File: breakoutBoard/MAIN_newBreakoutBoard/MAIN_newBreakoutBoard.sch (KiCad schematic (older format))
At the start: 3 parts, among them J1 Conn_02x06_Test_Pins, J2 Conn_02x06_Steering_Wheel_Qui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, J3 Conn_01x14

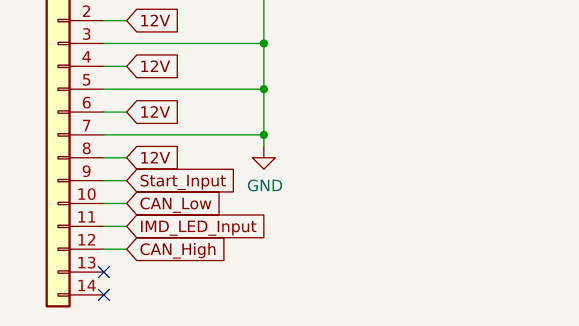
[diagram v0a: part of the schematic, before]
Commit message: Made use of entire ampseal connector
Had a late night ah ha momment;; Figured I would make use of all the pins on the ampseal connect and make it so we have the option to add another CAN node at the front of the car if need be.
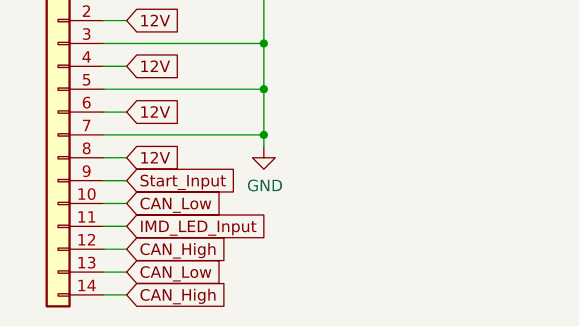
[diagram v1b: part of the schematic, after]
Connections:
- net CAN_High: now also J3.14 (Pin_14)
- net CAN_Low: now also J3.13 (Pin_13)
- no-connect marks 2 -> 0
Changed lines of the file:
@@
 EESchema Schematic File Version 4
+LIBS:MAIN_newBreakoutBoard-cache
 EELAYER 30 0
 EELAYER END
@@
 	0    -1   -1   0
 $EndComp
+Text GLabel 1400 3800 1    50   Input ~ 0
+12V
+Text GLabel 1800 3800 1    50   Input ~ 0
+CAN_Low
+Text GLabel 1900 3800 1    50   Input ~ 0
+CAN_High
+Text GLabel 1800 4500 3    50   Input ~ 0
+Start_Input
+Text GLabel 1900 4500 3    50   Input ~ 0
+IMD_LED_Input
+Wire Wire Line
+	1900 4500 1900 4400
+Wire Wire Line
+	1800 4500 1800 4400
+Wire Wire Line
+	1900 3800 1900 3900
+Wire Wire Line
+	1800 3800 1800 3900
+Wire Wire Line
+	1400 3800 1400 3850
+Wire Wire Line
+	1500 3900 1500 3850
+Wire Wire Line
+	1500 3850 1400 3850
+Connection ~ 1400 3850
+Wire Wire Line
+	1400 3850 1400 3900
+Wire Wire Line
+	1600 3900 1600 3850
+Wire Wire Line
+	1600 3850 1500 3850
+Connection ~ 1500 3850
+Wire Wire Line
+	1700 3900 1700 3850
+Wire Wire Line
+	1700 3850 1600 3850
+Connection ~ 1600 3850
+Wire Wire Line
+	1400 4500 1400 4450
+Wire Wire Line
+	1500 4400 1500 4450
+Wire Wire Line
+	1500 4450 1400 4450
+Connection ~ 1400 4450
+Wire Wire Line
+	1400 4450 1400 4400
+Wire Wire Line
+	1600 4400 1600 4450
+Wire Wire Line
+	1600 4450 1500 4450
+Connection ~ 1500 4450
+Wire Wire Line
+	1700 4400 1700 4450
+Wire Wire Line
+	1700 4450 1600 4450
+Connection ~ 1600 4450
+$Comp
+L Connector_Generic:Conn_02x06_Odd_Even J1
+U 1 1 5FAA108C
+P 1600 2300
+F 0 "J1" V 1696 1912 50  0000 R CNN
+F 1 "Conn_02x06_Test_Pins" V 1605 1912 50  0000 R CNN
+F 2 "Connector_PinSocket_2.54mm:PinSocket_2x06_P2.54mm_Vertical" H 1600 2300 50  0001 C CNN
+F 3 "~" H 1600 2300 50  0001 C CNN
+	1    1600 2300
+	0    -1   -1   0
+$EndComp
+Text GLabel 1400 1900 1    50   Input ~ 0
+12V
+Text GLabel 1800 1900 1    50   Input ~ 0
+CAN_Low
+Text GLabel 1900 1900 1    50   Input ~ 0
+CAN_High
+Text GLabel 1800 2600 3    50   Input ~ 0
+Start_Input
+Text GLabel 1900 2600 3    50   Input ~ 0
+IMD_LED_Input
+Wire Wire Line
+	1900 2600 1900 2500
+Wire Wire Line
+	1800 2600 1800 2500
+Wire Wire Line
+	1900 1900 1900 2000
+Wire Wire Line
+	1800 1900 1800 2000
+Wire Wire Line
+	1400 1900 1400 1950
+Wire Wire Line
+	1500 2000 1500 1950
+Wire Wire Line
+	1500 1950 1400 1950
+Connection ~ 1400 1950
+Wire Wire Line
+	1400 1950 1400 2000
+Wire Wire Line
+	1600 2000 1600 1950
+Wire Wire Line
+	1600 1950 1500 1950
+Connection ~ 1500 1950
+Wire Wire Line
+	1700 2000 1700 1950
+Wire Wire Line
+	1700 1950 1600 1950
+Connection ~ 1600 1950
+Wire Wire Line
+	1400 2600 1400 2550
+Wire Wire Line
+	1500 2500 1500 2550
+Wire Wire Line
+	1500 2550 1400 2550
+Connection ~ 1400 2550
+Wire Wire Line
+	1400 2550 1400 2500
+Wire Wire Line
+	1600 2500 1600 2550
+Wire Wire Line
+	1600 2550 1500 2550
+Connection ~ 1500 2550
+Wire Wire Line
+	1700 2500 1700 2550
+Wire Wire Line
+	1700 2550 1600 2550
+Connection ~ 1600 2550
+Text GLabel 1700 5650 2    50   Input ~ 0
+12V
+Text GLabel 1700 5850 2    50   Input ~ 0
+12V
+Text GLabel 1700 6050 2    50   Input ~ 0
+12V
+Text GLabel 1700 6250 2    50   Input ~ 0
+12V
+Text GLabel 1700 6350 2    50   Input ~ 0
+Start_Input
+Text GLabel 1700 6450 2    50   Input ~ 0
+CAN_Low
+Text GLabel 1700 6550 2    50   Input ~ 0
+IMD_LED_Input
+Text GLabel 1700 6650 2    50   Input ~ 0
+CAN_High
+Wire Wire Line
+	1700 5650 1600 5650
+Wire Wire Line
+	1700 5850 1600 5850
+Wire Wire Line
+	1700 6050 1600 6050
+Wire Wire Line
+	1700 6250 1600 6250
+Wire Wire Line
+	1600 6350 1700 6350
+Wire Wire Line
+	1700 6450 1600 6450
+Wire Wire Line
+	1600 6550 1700 6550
+Wire Wire Line
+	1700 6650 1600 6650
+$Comp
+L power:GND #PWR0101
+U 1 1 5FADA1A1
+P 1400 2600
+F 0 "#PWR0101" H 1400 2350 50  0001 C CNN
+F 1 "GND" H 1405 2427 50  0000 C CNN
+F 2 "" H 1400 2600 50  0001 C CNN
+F 3 "" H 1400 2600 50  0001 C CNN
+	1    1400 2600
+	1    0    0    -1
+$EndComp
+$Comp
+L power:GND #PWR0102
+U 1 1 5FADA758
+P 1400 4500
+F 0 "#PWR0102" H 1400 4250 50  0001 C CNN
+F 1 "GND" H 1405 4327 50  0000 C CNN
+F 2 "" H 1400 4500 50  0001 C CNN
+F 3 "" H 1400 4500 50  0001 C CNN
+	1    1400 4500
+	1    0    0    -1
+$EndComp
+$Comp
+L power:GND #PWR0103
+U 1 1 5FADAEC6
+P 2300 6200
+F 0 "#PWR0103" H 2300 5950 50  0001 C CNN
+F 1 "GND" H 2305 6027 50  0000 C CNN
+F 2 "" H 2300 6200 50  0001 C CNN
+F 3 "" H 2300 6200 50  0001 C CNN
+	1    2300 6200
+	1    0    0    -1
+$EndComp
+Wire Wire Line
+	2300 5550 2300 5750
+Wire Wire Line
+	1600 5550 2300 5550
+Wire Wire Line
+	1600 6150 2300 6150
+Connection ~ 2300 6150
+Wire Wire Line
+	1600 5950 2300 5950
+Connection ~ 2300 5950
+Wire Wire Line
+	2300 5950 2300 6150
+Wire Wire Line
+	1600 5750 2300 5750
+Connection ~ 2300 5750
+Wire Wire Line
+	2300 5750 2300 5950
+Wire Wire Line
+	2300 6150 2300 6200
+Text Notes 2150 2650 0    50   ~ 0
+NOTE: The corresponding symbol has a vertical orientation. \nWhile vertical pins can be used, the board was designed with\nintentions of using horizontal pins.
 $Comp
 L Connector_Generic:Conn_01x14 J3
@@
 	-1   0    0    -1
 $EndComp
-Text GLabel 1400 3800 1    50   Input ~ 0
-12V
-Text GLabel 1800 3800 1    50   Input ~ 0
-CAN_Low
-Text GLabel 1900 3800 1    50   Input ~ 0
-CAN_High
-Text GLabel 1800 4500 3    50   Input ~ 0
-Start_Input
-Text GLabel 1900 4500 3    50   Input ~ 0
-IMD_LED_Input
-Wire Wire Line
-	1900 4500 1900 4400
-Wire Wire Line
-	1800 4500 1800 4400
-Wire Wire Line
-	1900 3800 1900 3900
-Wire Wire Line
-	1800 3800 1800 3900
-Wire Wire Line
-	1400 3800 1400 3850
-Wire Wire Line
-	1500 3900 1500 3850
-Wire Wire Line
-	1500 3850 1400 3850
-Connection ~ 1400 3850
-Wire Wire Line
-	1400 3850 1400 3900
-Wire Wire Line
-	1600 3900 1600 3850
-Wire Wire Line
-	1600 3850 1500 3850
-Connection ~ 1500 3850
-Wire Wire Line
-	1700 3900 1700 3850
-Wire Wire Line
-	1700 3850 1600 3850
-Connection ~ 1600 3850
-Wire Wire Line
-	1400 4500 1400 4450
-Wire Wire Line
-	1500 4400 1500 4450
-Wire Wire Line
-	1500 4450 1400 4450
-Connection ~ 1400 4450
-Wire Wire Line
-	1400 4450 1400 4400
-Wire Wire Line
-	1600 4400 1600 4450
-Wire Wire Line
-	1600 4450 1500 4450
-Connection ~ 1500 4450
-Wire Wire Line
-	1700 4400 1700 4450
-Wire Wire Line
-	1700 4450 1600 4450
-Connection ~ 1600 4450
-$Comp
-L Connector_Generic:Conn_02x06_Odd_Even J1
-U 1 1 5FAA108C
-P 1600 2300
-F 0 "J1" V 1696 1912 50  0000 R CNN
-F 1 "Conn_02x06_Test_Pins" V 1605 1912 50  0000 R CNN
-F 2 "Connector_PinSocket_2.54mm:PinSocket_2x06_P2.54mm_Vertical" H 1600 2300 50  0001 C CNN
-F 3 "~" H 1600 2300 50  0001 C CNN
-	1    1600 2300
-	0    -1   -1   0
-$EndComp
-Text GLabel 1400 1900 1    50   Input ~ 0
-12V
-Text GLabel 1800 1900 1    50   Input ~ 0
-CAN_Low
-Text GLabel 1900 1900 1    50   Input ~ 0
-CAN_High
-Text GLabel 1800 2600 3    50   Input ~ 0
-Start_Input
-Text GLabel 1900 2600 3    50   Input ~ 0
-IMD_LED_Input
-Wire Wire Line
-	1900 2600 1900 2500
-Wire Wire Line
-	1800 2600 1800 2500
-Wire Wire Line
-	1900 1900 1900 2000
-Wire Wire Line
-	1800 1900 1800 2000
-Wire Wire Line
-	1400 1900 1400 1950
-Wire Wire Line
-	1500 2000 1500 1950
-Wire Wire Line
-	1500 1950 1400 1950
-Connection ~ 1400 1950
-Wire Wire Line
-	1400 1950 1400 2000
-Wire Wire Line
-	1600 2000 1600 1950
-Wire Wire Line
-	1600 1950 1500 1950
-Connection ~ 1500 1950
-Wire Wire Line
-	1700 2000 1700 1950
-Wire Wire Line
-	1700 1950 1600 1950
-Connection ~ 1600 1950
-Wire Wire Line
-	1400 2600 1400 2550
-Wire Wire Line
-	1500 2500 1500 2550
-Wire Wire Line
-	1500 2550 1400 2550
-Connection ~ 1400 2550
-Wire Wire Line
-	1400 2550 1400 2500
-Wire Wire Line
-	1600 2500 1600 2550
-Wire Wire Line
-	1600 2550 1500 2550
-Connection ~ 1500 2550
-Wire Wire Line
-	1700 2500 1700 2550
-Wire Wire Line
-	1700 2550 1600 2550
-Connection ~ 1600 2550
-Text GLabel 1700 5650 2    50   Input ~ 0
-12V
-Text GLabel 1700 5850 2    50   Input ~ 0
-12V
-Text GLabel 1700 6050 2    50   Input ~ 0
-12V
-Text GLabel 1700 6250 2    50   Input ~ 0
-12V
-Text GLabel 1700 6350 2    50   Input ~ 0
-Start_Input
-Text GLabel 1700 6450 2    50   Input ~ 0
-CAN_Low
-Text GLabel 1700 6550 2    50   Input ~ 0
-IMD_LED_Input
-Text GLabel 1700 6650 2    50   Input ~ 0
-CAN_High
-NoConn ~ 1600 6750
-NoConn ~ 1600 6850
-Wire Wire Line
-	1700 5650 1600 5650
-Wire Wire Line
-	1700 5850 1600 5850
-Wire Wire Line
-	1700 6050 1600 6050
-Wire Wire Line
-	1700 6250 1600 6250
-Wire Wire Line
-	1600 6350 1700 6350
-Wire Wire Line
-	1700 6450 1600 6450
-Wire Wire Line
-	1600 6550 1700 6550
-Wire Wire Line
-	1700 6650 1600 6650
-$Comp
-L power:GND #PWR0101
-U 1 1 5FADA1A1
-P 1400 2600
-F 0 "#PWR0101" H 1400 2350 50  0001 C CNN
-F 1 "GND" H 1405 2427 50  0000 C CNN
-F 2 "" H 1400 2600 50  0001 C CNN
-F 3 "" H 1400 2600 50  0001 C CNN
-	1    1400 2600
-	1    0    0    -1
-$EndComp
-$Comp
-L power:GND #PWR0102
-U 1 1 5FADA758
-P 1400 4500
-F 0 "#PWR0102" H 1400 4250 50  0001 C CNN
-F 1 "GND" H 1405 4327 50  0000 C CNN
-F 2 "" H 1400 4500 50  0001 C CNN
-F 3 "" H 1400 4500 50  0001 C CNN
-	1    1400 4500
-	1    0    0    -1
-$EndComp
-$Comp
-L power:GND #PWR0103
-U 1 1 5FADAEC6
-P 2300 6200
-F 0 "#PWR0103" H 2300 5950 50  0001 C CNN
-F 1 "GND" H 2305 6027 50  0000 C CNN
-F 2 "" H 2300 6200 50  0001 C CNN
-F 3 "" H 2300 6200 50  0001 C CNN
-	1    2300 6200
-	1    0    0    -1
-$EndComp
-Wire Wire Line
-	2300 5550 2300 5750
-Wire Wire Line
-	1600 5550 2300 5550
-Wire Wire Line
-	1600 6150 2300 6150
-Connection ~ 2300 6150
-Wire Wire Line
-	1600 5950 2300 5950
-Connection ~ 2300 5950
-Wire Wire Line
-	2300 5950 2300 6150
-Wire Wire Line
-	1600 5750 2300 5750
-Connection ~ 2300 5750
-Wire Wire Line
-	2300 5750 2300 5950
-Wire Wire Line
-	2300 6150 2300 6200
-Text Notes 2150 2650 0    50   ~ 0
-NOTE: The corresponding symbol has a vertical orientation. \nWhile vertical pins can be used, the board was designed with\nintentions of using horizontal pins.
+Text GLabel 1700 6750 2    50   Input ~ 0
+CAN_Low
+Text GLabel 1700 6850 2    50   Input ~ 0
+CAN_High
+Wire Wire Line
+	1600 6750 1700 6750
+Wire Wire Line
+	1600 6850 1700 6850
 $EndSCHEMATC
